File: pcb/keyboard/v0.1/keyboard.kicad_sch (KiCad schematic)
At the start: 113 parts, among them J1 USB2.0, J2 SWD, SW1 SPACE, SW13 TAB, SW14 Q, SW15 W, SW16 E, SW17 R, SW18 T, SW19 Y, SW2 SPACE, SW20 U, SW21 I, SW22 O, SW23 P, SW24 RETURN, SW25 CAPS, SW26 A, SW27 S, SW28 D, SW29 F, SW30 G, SW31 H, SW32 J, SW33 K, SW34 L, SW35 SEMI, SW36 QUOTE, SW37 LSHIFT, SW38 Z, SW39 X, SW40 C, SW41 V, SW42 B, SW43 N, SW44 M, SW45 COMMA, SW46 DOT, SW47 QUEST, SW48 RSHIFT, SW49 FN, SW50 LCTRL, SW51 LSUPER, SW52 LALT, SW54 RALT, SW55 RSUPER, SW56 MENU, SW57 RCTRL, SW59 C2, SW62 C5, U1 MDBT50Q-P1MV2, Y1 32.768

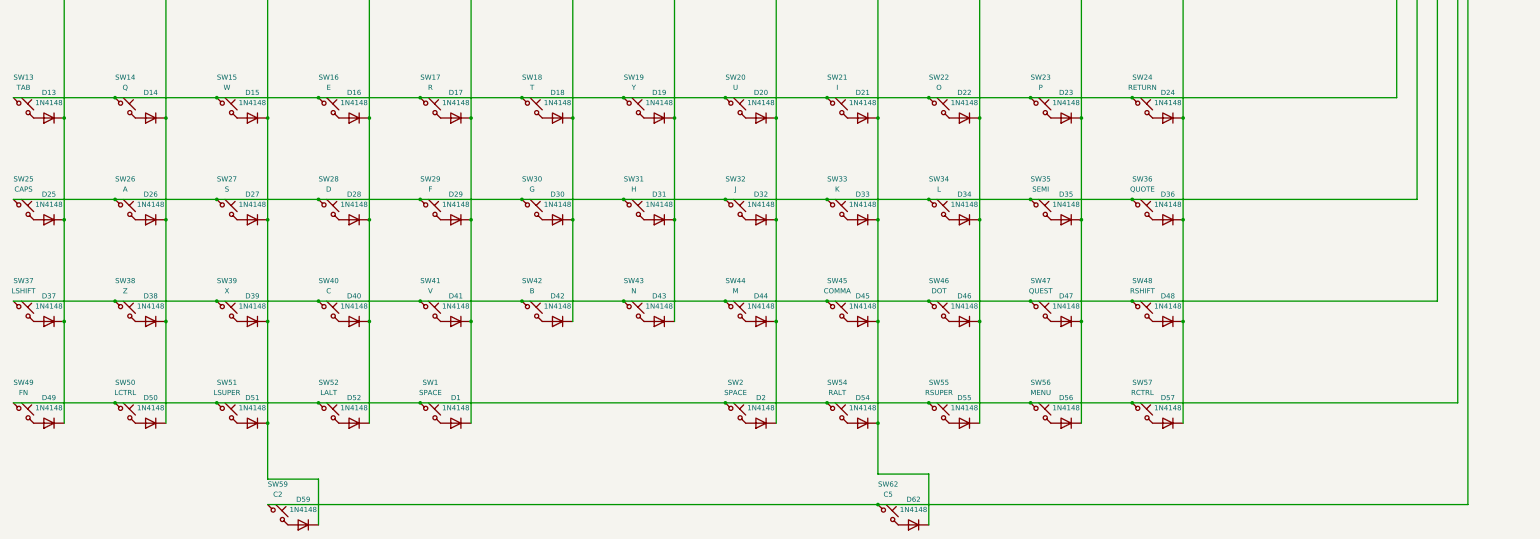
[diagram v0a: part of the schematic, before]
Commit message: New layout again. Also 7 macro keys now to fill the space
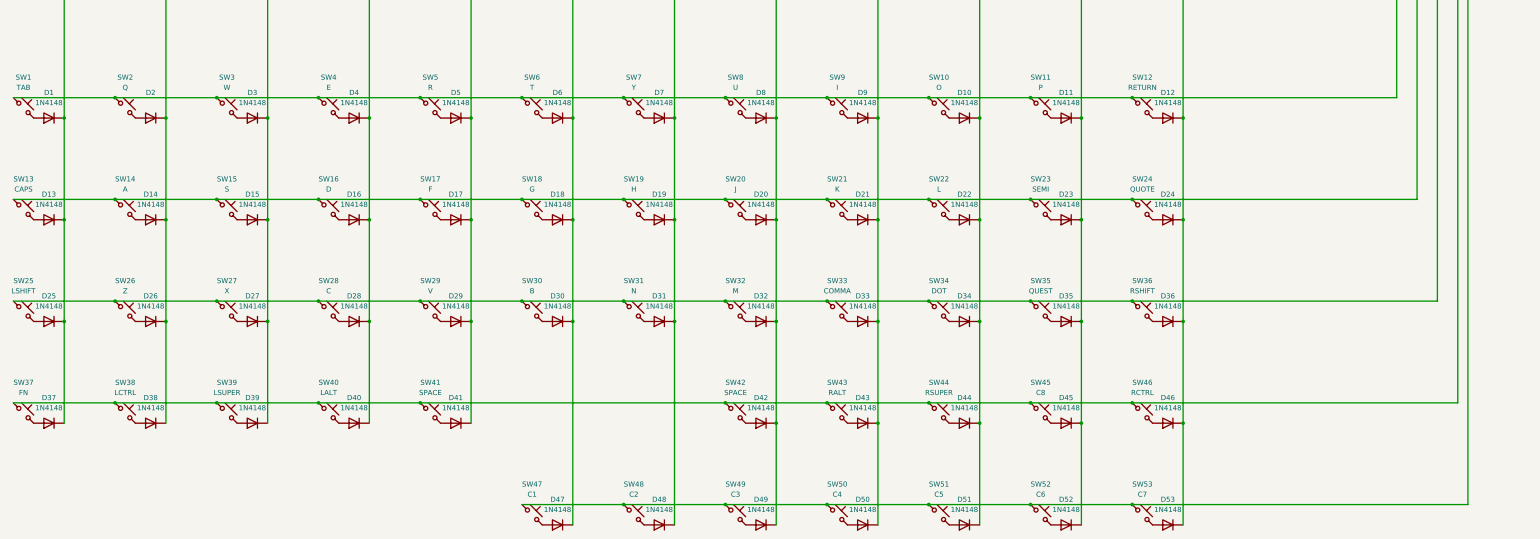
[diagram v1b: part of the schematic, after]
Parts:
- added D47, D49, D50, D52, D53: 1N4148, Diode_SMD:D_SOD-523, symbol Device:D
- added SW47: C1, TH-A1OC:tact_switch_4.5x4.5_PTS647, symbol TH-A10C:SW_Push_45deg
- added SW49: C3, TH-A1OC:tact_switch_4.5x4.5_PTS647, symbol TH-A10C:SW_Push_45deg
- added SW50: C4, TH-A1OC:tact_switch_4.5x4.5_PTS647, symbol TH-A10C:SW_Push_45deg
- added SW52: C6, TH-A1OC:tact_switch_4.5x4.5_PTS647, symbol TH-A10C:SW_Push_45deg
- added SW53: C7, TH-A1OC:tact_switch_4.5x4.5_PTS647, symbol TH-A10C:SW_Push_45deg
- SW45: renamed from SW56; value MENU -> C8
- renumbered D13 to D1, D22 to D10, D23 to D11, D24 to D12, D25 to D13, D26 to D14, D27 to D15, D28 to D16, D29 to D17, D30 to D18, D31 to D19, D14 to D2, D32 to D20, D33 to D21, D34 to D22, D35 to D23, D36 to D24, D37 to D25, D38 to D26, D39 to D27, D40 to D28, D41 to D29, D15 to D3, D42 to D30, D43 to D31, D44 to D32, D45 to D33, D46 to D34, D47 to D35, D48 to D36, D49 to D37, D50 to D38, D51 to D39, D16 to D4, D52 to D40, D1 to D41, D2 to D42, D54 to D43, D55 to D44, D56 to D45, D57 to D46, D59 to D48, D17 to D5, D62 to D51, D18 to D6, D19 to D7, D20 to D8, D21 to D9, SW13 to SW1, SW22 to SW10, SW23 to SW11, SW24 to SW12, SW25 to SW13, SW26 to SW14, SW27 to SW15, SW28 to SW16, SW29 to SW17, SW30 to SW18, SW31 to SW19, SW14 to SW2, SW32 to SW20, SW33 to SW21, SW34 to SW22, SW35 to SW23, SW36 to SW24, SW37 to SW25, SW38 to SW26, SW39 to SW27, SW40 to SW28, SW41 to SW29, SW15 to SW3, SW42 to SW30, SW43 to SW31, SW44 to SW32, SW45 to SW33, SW46 to SW34, SW47 to SW35, SW48 to SW36, SW49 to SW37, SW50 to SW38, SW51 to SW39, SW16 to SW4, SW52 to SW40, SW1 to SW41, SW2 to SW42, SW54 to SW43, SW55 to SW44, SW57 to SW46, SW59 to SW48, SW17 to SW5, SW62 to SW51, SW18 to SW6, SW19 to SW7, SW20 to SW8, SW21 to SW9
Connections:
- net INPUT10: now also D51.1 (K)
- net INPUT11: now also D52.1 (K)
- net INPUT12: now also D53.1 (K)
- net INPUT3: no longer D48.1 (K)
- net INPUT6: now also D47.1 (K)
- net INPUT7: now also D48.1 (K)
- net INPUT8: now also D49.1 (K)
- net INPUT9: now also D50.1 (K); no longer D51.1 (K)
- net SOURCE5: now also SW47.1, SW49.1, SW50.1, SW52.1, SW53.1
- new net: D53.2 (A), SW53.2
- new net: D52.2 (A), SW52.2
- new net: D47.2 (A), SW47.2
- new net: D50.2 (A), SW50.2
- new net: D49.2 (A), SW49.2
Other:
- moved on the sheet: D48, D51, SW48, SW51
